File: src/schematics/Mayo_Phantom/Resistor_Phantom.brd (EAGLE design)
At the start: 147.3 x 36.5 mm, 193 parts, among them K1 AQY221R2V, K2 AQY221R2V, K3 AQY221R2V, X1 DSUBIN

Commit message: Resistor Phantom
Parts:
- removed D3: 1N4148DO35-7, diode:DO35-7
- removed X2: (no value), con-molex:KK-156-4
- added D1: 1N4148, diode:SOD123
- added J2: 22-27-2041-04, con-molex:6410-04
- D2: value 1N4148DO35-7 -> 1N4148; device diode:DO35-7 -> diode:SOD123
- moved D2 93.5 mm to (-52.0, 47.5), flipped to the bottom, turned to 270 degrees
- moved R178 92.9 mm to (-63.6, 46.8), flipped to the bottom, turned to 90 degrees
- moved R177 91.1 mm to (-62.0, 46.8), flipped to the bottom, turned to 270 degrees
- moved R176 89.6 mm to (-60.5, 46.8), flipped to the bottom, turned to 90 degrees
- moved R167 82.3 mm to (-70.5, 46.7), flipped to the bottom
- moved R166 74.8 mm to (-76.3, 51.9), flipped to the bottom, turned to 270 degrees
- moved Q2 74.6 mm to (-73.7, 47.9), flipped to the bottom
- moved K3 74.0 mm to (-56.7, 46.8), flipped to the bottom
- moved JP1 73.7 mm to (16.7, 34.3)
- moved L3 71.7 mm to (-55.0, 49.5), flipped to the bottom
- moved L2 70.8 mm to (-79.5, 49.5), flipped to the bottom
- moved R169 68.3 mm to (-51.9, 51.8), flipped to the bottom, turned to 270 degrees
- moved K2 67.8 mm to (-81.2, 46.9), flipped to the bottom
- moved R163 67.4 mm to (-61.5, 68.0), flipped to the bottom, turned to 270 degrees
- moved R162 66.5 mm to (-46.8, 69.4)
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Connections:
- net 5V: now also J2.1; no longer X2.1
- net ARD_GND: now also D1.A, J2.3; no longer D3.A, X2.2
- net IN: now also J2.2; no longer X2.3
- net N$21: now also D1.C; no longer D2.C
- net N$39: now also D2.C; no longer D3.C
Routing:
- net GND: track 0.00 -> 109.8 mm, vias 0 -> 1
- net ARD_GND: track 0.00 -> 15.5 mm
- net 5V: track 0.00 -> 14.8 mm
- net SW_IN1: track 0.00 -> 9.68 mm, vias 0 -> 1
- net N$35: track 0.00 -> 7.22 mm
- net N$21: track 0.00 -> 7.03 mm
- net E28: track 0.00 -> 6.00 mm
- net E26: track 0.00 -> 6.00 mm
- net E25: track 0.00 -> 5.99 mm
- net E32: track 0.00 -> 5.98 mm
- net E27: track 0.00 -> 5.98 mm
- net E30: track 0.00 -> 5.98 mm
- net E29: track 0.00 -> 5.98 mm
- net E2: track 0.00 -> 5.98 mm
- net E31: track 0.00 -> 5.97 mm
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
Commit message: Resistor Phantom
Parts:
- moved JP1 45.1 mm to (-26.8, 46.3)
- moved R169 4.50 mm to (-47.4, 51.8), turned to 0 degrees
- moved D2 4.03 mm to (-48.0, 48.0)
- moved J2 4.03 mm to (-35.0, 51.0)
- moved K3 4.03 mm to (-52.7, 47.3)
- moved L3 4.03 mm to (-51.0, 50.0)
- moved Q3 4.03 mm to (-45.2, 48.3)
- moved R170 4.03 mm to (-41.9, 47.2)
- moved R176 4.03 mm to (-56.5, 47.3)
- moved R177 4.03 mm to (-58.0, 47.3)
- moved R178 4.03 mm to (-59.6, 47.3)
- moved R166 0.71 mm to (-75.8, 51.4), turned to 0 degrees
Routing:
- net GND: track 109.8 -> 233.5 mm, vias 1 -> 3
- net ARD_GND: track 15.5 -> 125.6 mm, vias 0 -> 1
- net IN: track 1.05 -> 90.0 mm, vias 0 -> 2
- net N$20: track 3.44 -> 91.2 mm, vias 0 -> 2
- net 5V: track 14.8 -> 97.5 mm
- net E56: track 3.59 -> 81.2 mm, vias 0 -> 2
- net N$2: track 3.31 -> 79.6 mm, vias 0 -> 2
- net E38: track 3.47 -> 65.7 mm, vias 0 -> 2
- net SW_IN2: track 5.22 -> 10.5 mm, vias 0 -> 1
- net SW_IN3: track 4.78 -> 9.33 mm, vias 0 -> 1
- net N$39: track 5.17 -> 7.09 mm
- added copper zone on layer 1, net N$32
- added copper zone on layer 16, net N$50
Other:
- board size 147.3 x 36.5 mm -> 284.7 x 43 mm

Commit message: Resistor Phantom
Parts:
- removed D1, D2, D4: 1N4148, diode:SOD123
- removed J2: 22-27-2041-04, con-molex:6410-04
- removed L1, L2, L3: BLM15H0805MAYO, inductors:0805
- removed Q1, Q2, Q3: (no value), semicon-smd-ipc:SOT23
- removed R161, R166, R169: 820, rcl:R0402
- removed R162, R167, R170: 3k, rcl:R0402
- added J1: 22-27-2041-04, con-molex:6410-04
- moved JP1 7.21 mm to (-22.8, 40.3)
- moved K1 4.00 mm to (-57.4, 73.3)
- moved R163 4.00 mm to (-61.5, 72.0)
- moved R164 4.00 mm to (-63.0, 72.0)
- moved R165 4.00 mm to (-64.5, 72.0)
- moved R168 4.00 mm to (-66.0, 72.0)
- moved R171 4.00 mm to (-67.5, 72.0)
- moved R138 3.20 mm to (-58.2, 79.0)
- moved R141 3.20 mm to (-50.2, 79.0)
- moved R142 3.20 mm to (-47.2, 79.0)
- moved R143 3.20 mm to (-44.4, 79.0)
- moved R147 3.20 mm to (-33.5, 79.0)
- moved R136 3.20 mm to (-63.8, 79.0)
- moved R137 3.20 mm to (-61.1, 79.0)
- moved R139 3.20 mm to (-55.6, 79.0)
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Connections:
- removed net 5V: J2.1, R161.1, R166.1, R169.1
- removed net IN: J2.2, R162.1, R167.1, R170.1
- removed net N$11: K2.1, L2.2
- removed net N$21: D1.C, L2.1, Q2.3, R166.2
- removed net N$27: K1.1, L1.2
- removed net N$35: D4.C, L1.1, Q1.3, R161.2
- removed net N$36: Q2.1, R167.2
- removed net N$37: Q1.1, R162.2
- removed net N$38: K3.1, L3.2
- removed net N$39: D2.C, L3.1, Q3.3, R169.2
- removed net N$40: Q3.1, R170.2
- new net IN1: J1.1, K1.1
- new net IN2: J1.2, K2.1
- new net IN3: J1.3, K3.1
- net ARD_GND: now also J1.4; no longer D1.A, D2.A, D4.A, J2.3, Q1.2, Q2.2, Q3.2
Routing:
- net 5V: track 97.5 -> 0.00 mm
- net IN: track 90.0 -> 0.00 mm, vias 2 -> 0
- net IN1: track 0.00 -> 57.5 mm
- net IN2: track 0.00 -> 44.8 mm
- net GND: track 233.5 -> 193.1 mm
- net IN3: track 0.00 -> 15.4 mm
- net N$21: track 7.24 -> 0.00 mm
- net N$35: track 7.22 -> 0.00 mm
- net N$39: track 7.09 -> 0.00 mm
- net N$2: track 79.6 -> 85.8 mm
- net N$20: track 91.2 -> 97.4 mm
- net N$27: track 3.55 -> 0.00 mm
- net N$38: track 3.27 -> 0.00 mm
- net N$11: track 3.11 -> 0.00 mm
- net E56: track 81.2 -> 84.1 mm
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- added copper zone on layer 1, net GND
- added copper zone on layer 16, net GND
- removed copper zone on layer 1, net N$32
- removed copper zone on layer 16, net N$50
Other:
- board size 284.7 x 43 mm -> 76 x 45 mm
- board text added: "(ch 10)"
- board text added: "(ch 20)"
- board text added: "(ch 30)"
- board text added: "0.1%"
- board text added: "1"
- board text added: "1.0%"
- board text added: "10"
- board text added: "10%"
- board text added: "15"
- board text added: "19"
- board text added: "20"
- board text added: "25"
- board text added: "32"
- board text added: "5"
- board text added: "Ard Gnd"
- board text removed: "DEBUG PHANTOM"
- board text removed: "JIMMY 2015"
- board text removed: "Please dont calibrate using this"

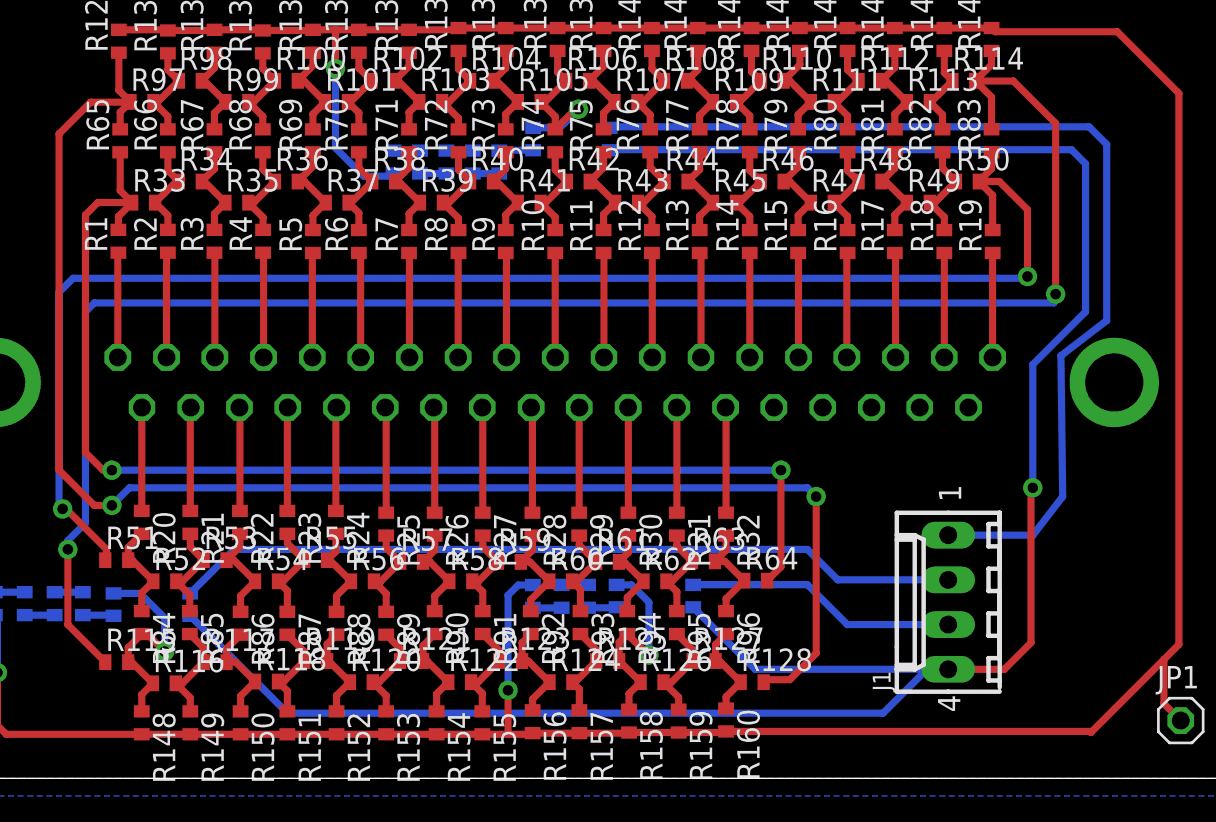
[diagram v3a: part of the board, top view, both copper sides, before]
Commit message: Resistor Phantom v1
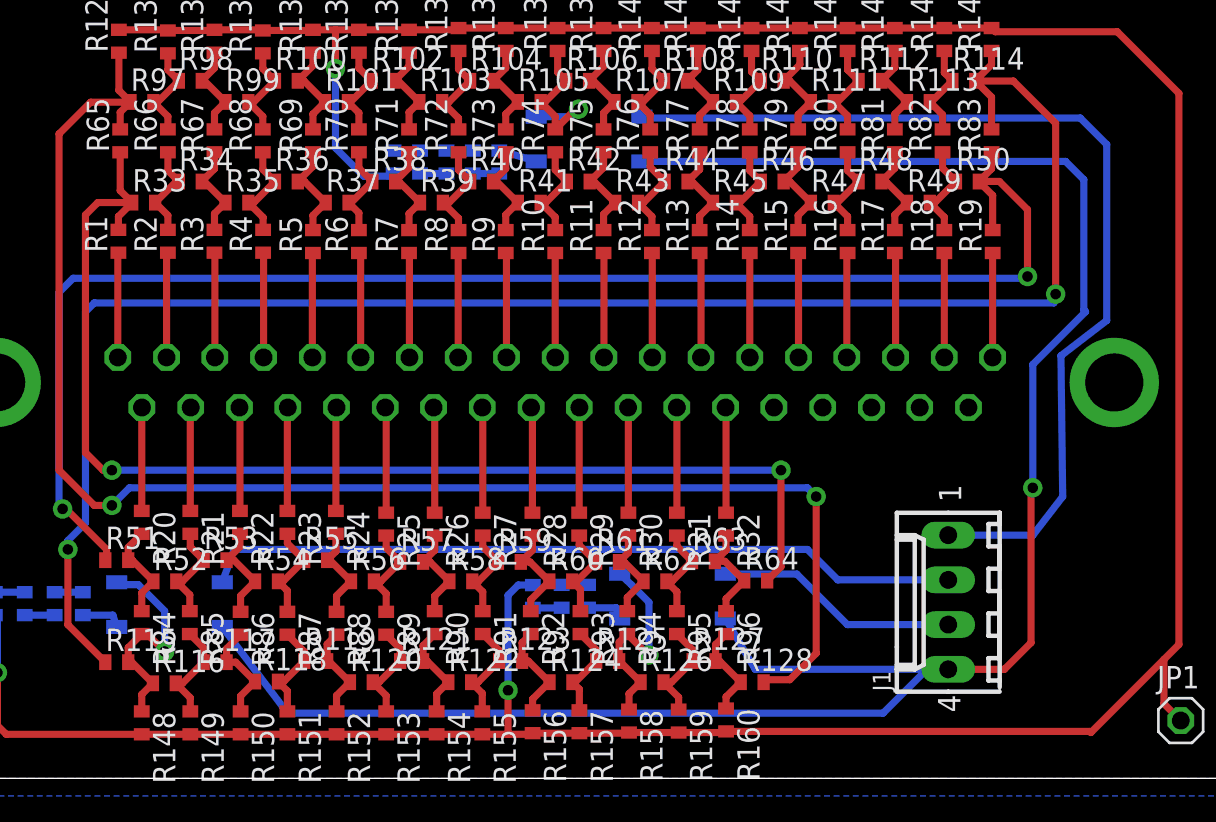
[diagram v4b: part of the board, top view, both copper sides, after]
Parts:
- K1, K2, K3: value AQY221R2V -> AQY22SOP; device relay:SSOP4 -> relay:SOP04
- R168: value 90k -> 75k
- R171: value 9k -> 24k
- moved K1 1.00 mm to (-56.4, 73.3), turned to 270 degrees
- moved K2 1.00 mm to (-80.2, 46.9), turned to 270 degrees
- moved K3 1.00 mm to (-51.7, 47.3), turned to 270 degrees
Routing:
- net ARD_GND: track 123.5 -> 117.5 mm
- net IN1: track 57.5 -> 55.9 mm
- net IN3: track 15.4 -> 13.9 mm
- net IN2: track 44.8 -> 43.3 mm
- net SW_OUT2: track 1.76 -> 2.41 mm
- net SW_OUT3: track 1.63 -> 2.23 mm
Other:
- board text added: "Fast Neural Phantom"
- board text removed: "1"
- board text removed: "10"
- board text removed: "15"
- board text removed: "19"
- board text removed: "20"
- board text removed: "25"
- board text removed: "32"
- board text removed: "5"

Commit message: changed resistor values in schematic
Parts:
- R163, R164, R165: value 300k -> 10k
- R168: value 75k -> 10k
- R171: value 24k -> 10k
- R172, R173: value 30k -> 2k
- R174: value 30k -> 500
- R175: value 9k -> 500
- R176, R177: value 3k -> 100
- R178: value 3k -> 200
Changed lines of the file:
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@@
 <attribute name="OC_FARNELL" value="unknown" x="-51.6614" y="47.3474" size="1.778" layer="28" rot="MR270" display="off"/>
 </element>
-<element name="R163" library="rcl" package="R0402" value="300k" x="-61.5" y="72" rot="MR270"/>
-<element name="R164" library="rcl" package="R0402" value="300k" x="-63" y="72" rot="MR270"/>
-<element name="R165" library="rcl" package="R0402" value="300k" x="-64.5" y="72" rot="MR270"/>
-<element name="R168" library="rcl" package="R0402" value="75k" x="-66" y="72" rot="MR270"/>
-<element name="R171" library="rcl" package="R0402" value="24k" x="-67.5" y="72" rot="MR270"/>
-<element name="R172" library="rcl" package="R0402" value="30k" x="-85.1486" y="46.9196" rot="MR90"/>
-<element name="R173" library="rcl" package="R0402" value="30k" x="-86.7486" y="46.9196" rot="MR90"/>
-<element name="R174" library="rcl" package="R0402" value="30k" x="-88.4486" y="46.9196" rot="MR90"/>
-<element name="R175" library="rcl" package="R0402" value="9k" x="-90.1486" y="46.9196" rot="MR90"/>
-<element name="R176" library="rcl" package="R0402" value="3k" x="-56.4545" y="47.3366" rot="MR90"/>
-<element name="R177" library="rcl" package="R0402" value="3k" x="-57.9545" y="47.3366" rot="MR270"/>
-<element name="R178" library="rcl" package="R0402" value="3k" x="-59.5911" y="47.3268" rot="MR90"/>
+<element name="R163" library="rcl" package="R0402" value="10k" x="-61.5" y="72" rot="MR270"/>
+<element name="R164" library="rcl" package="R0402" value="10k" x="-63" y="72" rot="MR270"/>
+<element name="R165" library="rcl" package="R0402" value="10k" x="-64.5" y="72" rot="MR270"/>
+<element name="R168" library="rcl" package="R0402" value="10k" x="-66" y="72" rot="MR270"/>
+<element name="R171" library="rcl" package="R0402" value="10k" x="-67.5" y="72" rot="MR270"/>
+<element name="R172" library="rcl" package="R0402" value="2k" x="-85.1486" y="46.9196" rot="MR90"/>
+<element name="R173" library="rcl" package="R0402" value="2k" x="-86.7486" y="46.9196" rot="MR90"/>
+<element name="R174" library="rcl" package="R0402" value="500" x="-88.4486" y="46.9196" rot="MR90"/>
+<element name="R175" library="rcl" package="R0402" value="500" x="-90.1486" y="46.9196" rot="MR90"/>
+<element name="R176" library="rcl" package="R0402" value="100" x="-56.4545" y="47.3366" rot="MR90"/>
+<element name="R177" library="rcl" package="R0402" value="100" x="-57.9545" y="47.3366" rot="MR270"/>
+<element name="R178" library="rcl" package="R0402" value="200" x="-59.5911" y="47.3268" rot="MR90"/>
 <element name="J1" library="con-molex" package="6410-04" value="22-27-2041-04" x="-36" y="47" smashed="yes" rot="R90">
 <attribute name="OC_NEWARK" value="unknown" x="-36" y="47" size="1.778" layer="27" rot="R90" display="off"/>
